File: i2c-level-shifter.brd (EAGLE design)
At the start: 23.5 x 23.5 mm, 12 parts, among them IC1 LP298XS, Q1 MMBF170, Q2 MMBF170

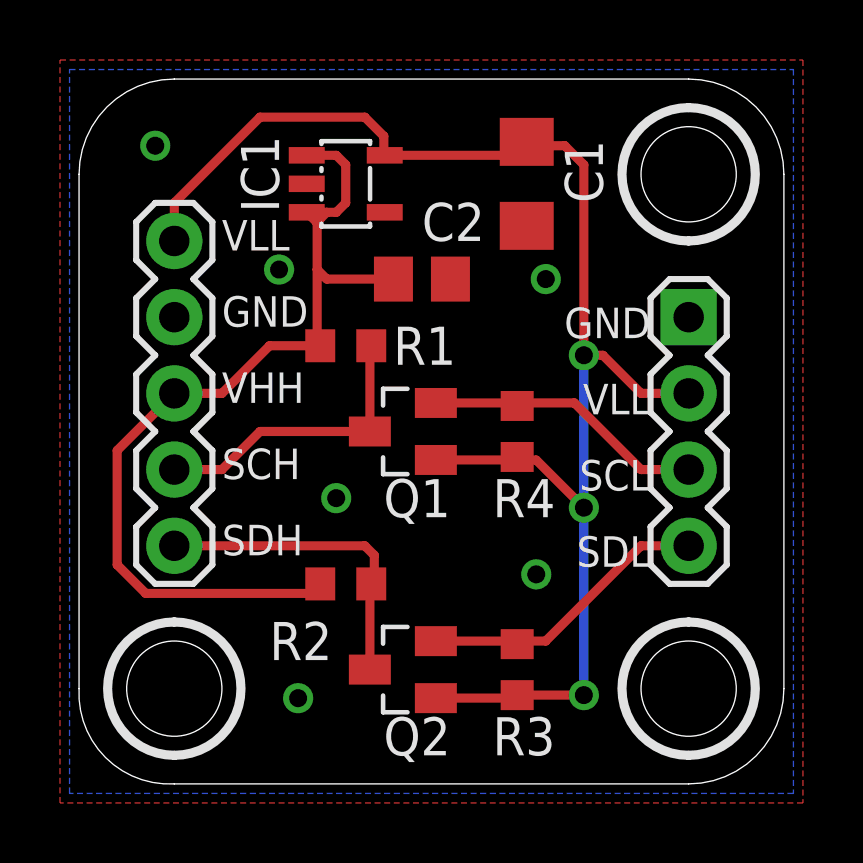
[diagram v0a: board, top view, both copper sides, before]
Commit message: reversed headers
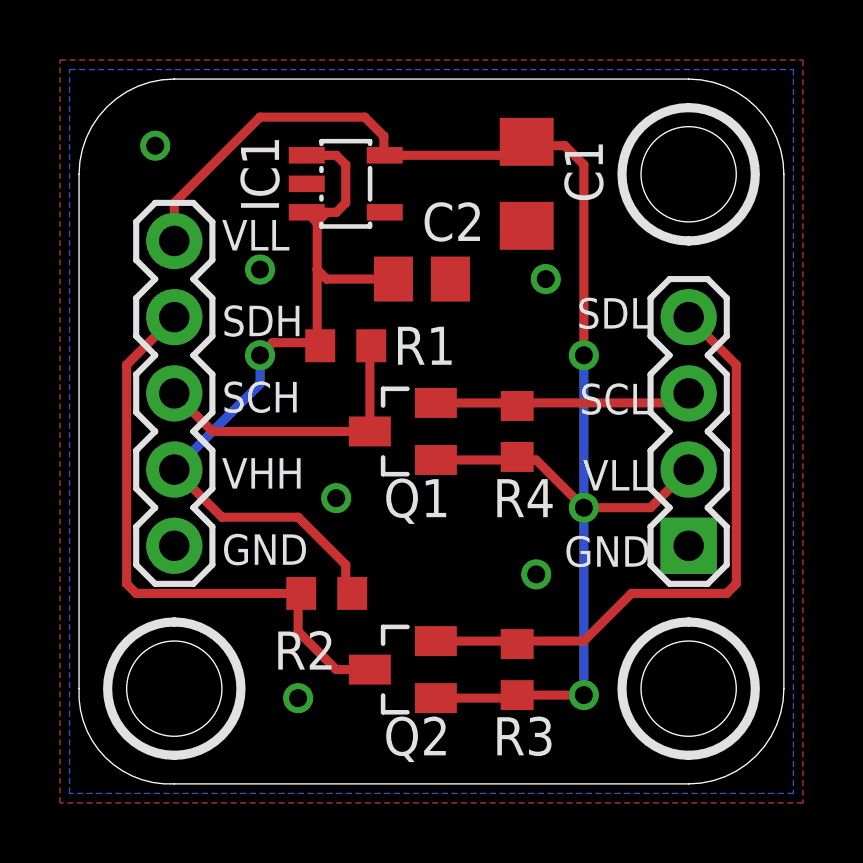
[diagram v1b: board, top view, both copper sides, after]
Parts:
- moved JP2 7.62 mm to (20.3, 7.94), turned to 90 degrees
- moved R2 0.71 mm to (8.26, 6.35), turned to 180 degrees
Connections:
- net GND: now also JP1.5; no longer JP1.2
- net SCH: now also JP1.3; no longer JP1.4
- net SDH: now also JP1.2; no longer JP1.5
- net VHH: now also JP1.4; no longer JP1.3
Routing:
- net SCL: track 9.82 -> 20.4 mm
- net SDH: track 10.7 -> 19.7 mm
- net VHH: track 31.1 -> 26.9 mm, vias 0 -> 1
- net SDL: track 9.43 -> 8.64 mm
